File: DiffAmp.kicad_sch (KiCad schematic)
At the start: 9 parts, among them U4 LMH6552MA

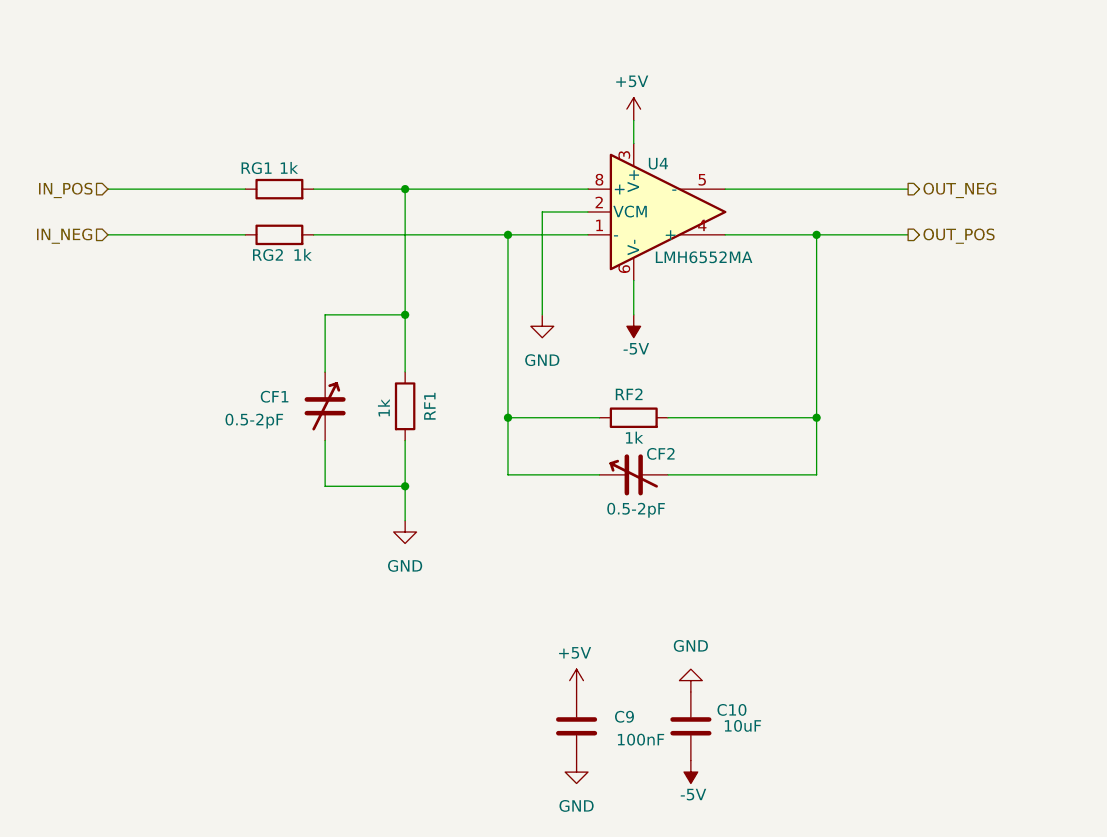
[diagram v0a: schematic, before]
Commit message: DRC completed. Need to add some 3D models.
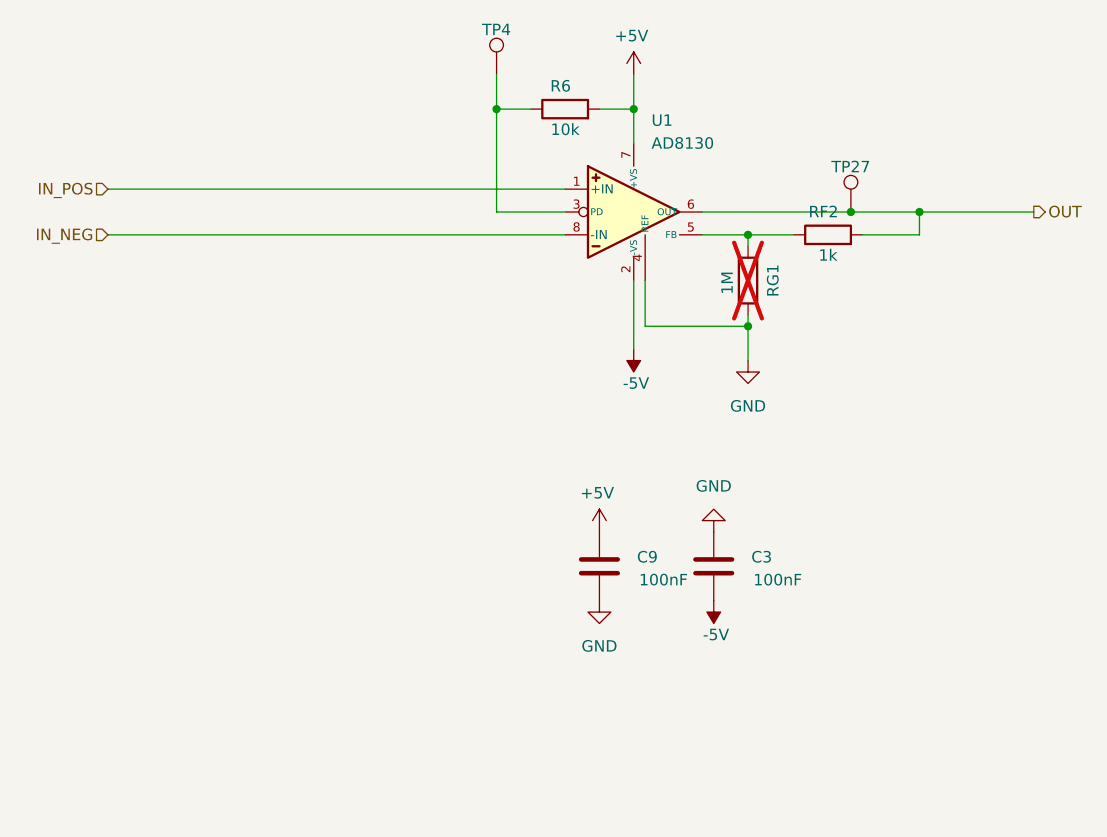
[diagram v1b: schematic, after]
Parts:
- removed C10: 10uF, Capacitor_SMD:C_0805_2012Metric, symbol Device:C
- removed CF1, CF2: 0.5-2pF, Capacitor_SMD:C_Trimmer_Murata_TZB4-B, symbol Device:C_Variable
- removed RG1, RG2: 1k, Resistor_SMD:R_0603_1608Metric, symbol Device:R
- removed U4: LMH6552MA, Package_SO:SOIC-8_3.9x4.9mm_P1.27mm, symbol Amplifier_Operational:LMH6551MA
- added C3: 100nF, Capacitor_SMD:C_0402_1005Metric_Pad0.74x0.62mm_HandSolder, symbol Device:C
- added R6: 10k, Resistor_SMD:R_0402_1005Metric_Pad0.72x0.64mm_HandSolder, symbol Device:R
- added TP27, TP4: TP, TestPoint:TestPoint_Pad_D1.0mm, symbol Connector:TestPoint
- added U1: AD8130, Package_SO:SOIC-8_3.9x4.9mm_P1.27mm, symbol ProjectLib:AD8130
- C9: footprint Capacitor_SMD:C_0603_1608Metric -> Capacitor_SMD:C_0402_1005Metric_Pad0.74x0.62mm_HandSolder
- RF2: footprint Resistor_SMD:R_0603_1608Metric -> Resistor_SMD:R_0402_1005Metric_Pad0.72x0.64mm_HandSolder
- RG1: renamed from RF1; value 1k -> 1M; footprint Resistor_SMD:R_0603_1608Metric -> Resistor_SMD:R_0402_1005Metric_Pad0.72x0.64mm_HandSolder; now not fitted
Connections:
- net +5V: now also R6.2, U1.7 (+VS)
- net -5V: now also C3.2, U1.2 (-VS)
- net GND: now also C3.1, U1.4 (REF)
- net IN_NEG: now also U1.8 (-IN)
- net IN_POS: now also U1.1 (+IN)
- net at RF2.1: now also RG1.1, U1.5 (FB)
- net OUT_POS renamed OUT
- net OUT: now also TP27.1, U1.6 (OUT)
- new net: R6.1, TP4.1, U1.3 (PD)
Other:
- moved on the sheet: C9, RF2

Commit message: R1 sent to JLCPCB
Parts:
- C3, C9: JLCPCB# (none) -> C60474
- R6: JLCPCB# (none) -> C25744
- RF2: JLCPCB# (none) -> C11702
- TP27, TP4: now left out of the parts list
- U1: JLCPCB# (none) -> C41661
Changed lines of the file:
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@@
 		(unit 1)
 		(exclude_from_sim no)
-		(in_bom yes)
+		(in_bom no)
 		(on_board yes)
 		(dnp no)
@@
 			)
 		)
+		(property "JLCPCB#" ""
+			(at 116.84 78.74 0)
+			(effects
+				(font
+					(size 1.27 1.27)
+				)
+				(hide yes)
+			)
+		)
 		(pin "1"
 		)
@@
 			)
 		)
+		(property "JLCPCB#" "C25744"
+			(at 124.46 82.55 90)
+			(effects
+				(font
+					(size 1.27 1.27)
+				)
+				(hide yes)
+			)
+		)
 		(pin "1"
 		)
@@
 		)
 		(property "Voltage" "16V"
+			(at 128.27 133.35 0)
+			(effects
+				(font
+					(size 1.27 1.27)
+				)
+				(hide yes)
+			)
+		)
+		(property "JLCPCB#" "C60474"
 			(at 128.27 133.35 0)
 			(effects
@@
 			)
 		)
+		(property "JLCPCB#" "C60474"
+			(at 140.97 133.35 0)
+			(effects
+				(font
+					(size 1.27 1.27)
+				)
+				(hide yes)
+			)
+		)
 		(pin "1"
 		)
@@
 			)
 		)
+		(property "JLCPCB#" "C11702"
+			(at 153.67 96.52 90)
+			(effects
+				(font
+					(size 1.27 1.27)
+				)
+				(hide yes)
+			)
+		)
 		(pin "1"
 		)
@@
 		(unit 1)
 		(exclude_from_sim no)
-		(in_bom yes)
+		(in_bom no)
 		(on_board yes)
 		(dnp no)
@@
 		)
 		(property "Description" "Test point - Input positive"
+			(at 156.21 93.98 0)
+			(effects
+				(font
+					(size 1.27 1.27)
+				)
+				(hide yes)
+			)
+		)
+		(property "JLCPCB#" ""
 			(at 156.21 93.98 0)
 			(effects
@@
 			)
 		)
+		(property "JLCPCB#" "C41661"
+			(at 132.08 93.98 0)
+			(effects
+				(font
+					(size 1.27 1.27)
+				)
+				(hide yes)
+			)
+		)
 		(pin "5"
 		)
@@
 			(effects
 				(font
+					(size 1.27 1.27)
+				)
+				(hide yes)
+			)
+		)
+		(property "JLCPCB#" ""
+			(at 144.78 101.6 90)
+			(effects
+				(font
